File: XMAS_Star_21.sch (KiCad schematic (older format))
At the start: 60 parts, among them J1 USB_B_Micro, J2 Conn_02x01, J3 Conn_01x03_Female, Q1 Q_PMOS_GDS, Q2 FS8205a, SW1 SW_SPDT, U1 ATtiny1607-M, U2 AW9523b, U4 TP4056X-UserLibray, U5 DW01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

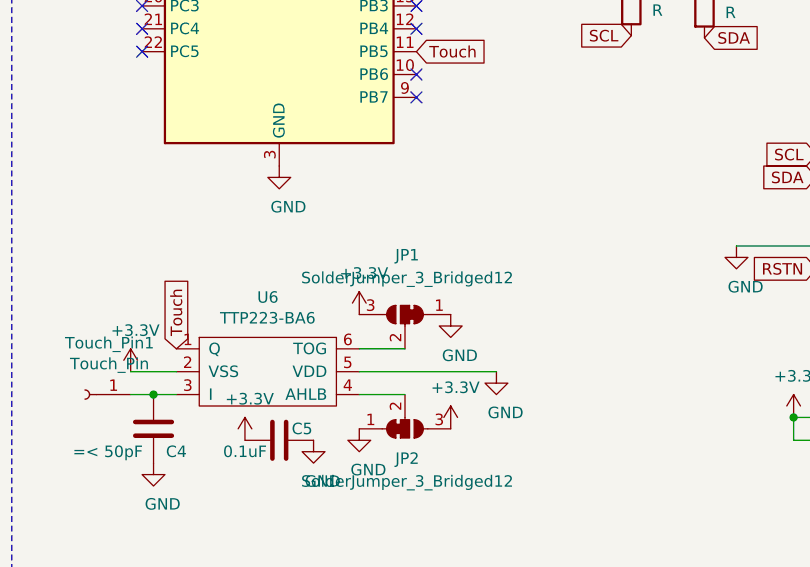
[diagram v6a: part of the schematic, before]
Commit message: further shaping of the code and change TTP223 from direct to toggle output
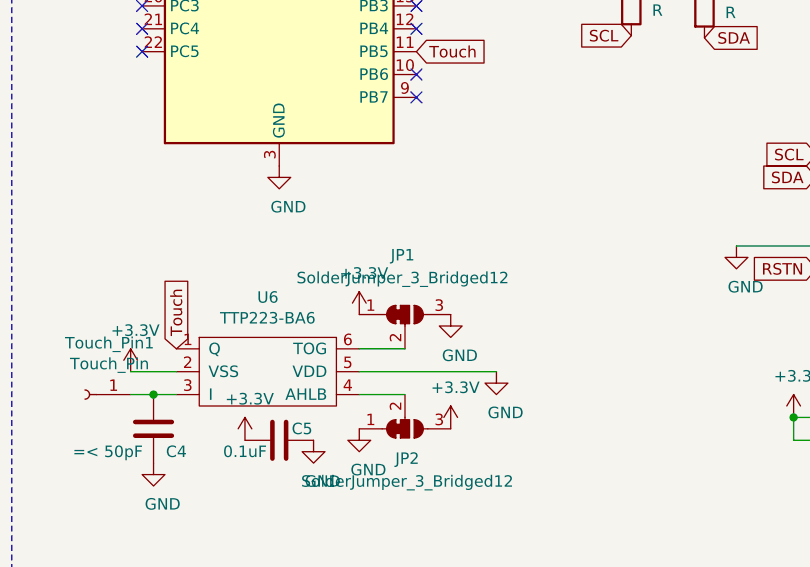
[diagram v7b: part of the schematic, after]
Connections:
- net +3V3: now also JP1.1 (A); no longer JP1.3 (B)
- net GND: now also JP1.3 (B); no longer JP1.1 (A)
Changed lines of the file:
@@
 	7300 5450 7100 5450
-$Comp
-L power:+3.3V #PWR035
-U 1 1 5FF4CA2A
-P 7100 5100
-F 0 "#PWR035" H 7100 4950 50  0001 C CNN
-F 1 "+3.3V" H 7120 5280 50  0000 C CNN
-F 2 "" H 7100 5100 50  0001 C CNN
-F 3 "" H 7100 5100 50  0001 C CNN
-	1    7100 5100
-	1    0    0    -1
-$EndComp
 $Comp
 L power:+3.3V #PWR040
@@
 F 3 "~" H 7300 5100 50  0001 C CNN
 	1    7300 5100
-	-1   0    0    -1
+	1    0    0    -1
 $EndComp
 $Comp
@@
 	1    0    0    -1
 $EndComp
+$Comp
+L power:+3.3V #PWR035
+U 1 1 5FF4CA2A
+P 7100 5100
+F 0 "#PWR035" H 7100 4950 50  0001 C CNN
+F 1 "+3.3V" H 7120 5280 50  0000 C CNN
+F 2 "" H 7100 5100 50  0001 C CNN
+F 3 "" H 7100 5100 50  0001 C CNN
+	1    7100 5100
+	1    0    0    -1
+$EndComp
